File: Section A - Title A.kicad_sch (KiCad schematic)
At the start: 0 parts

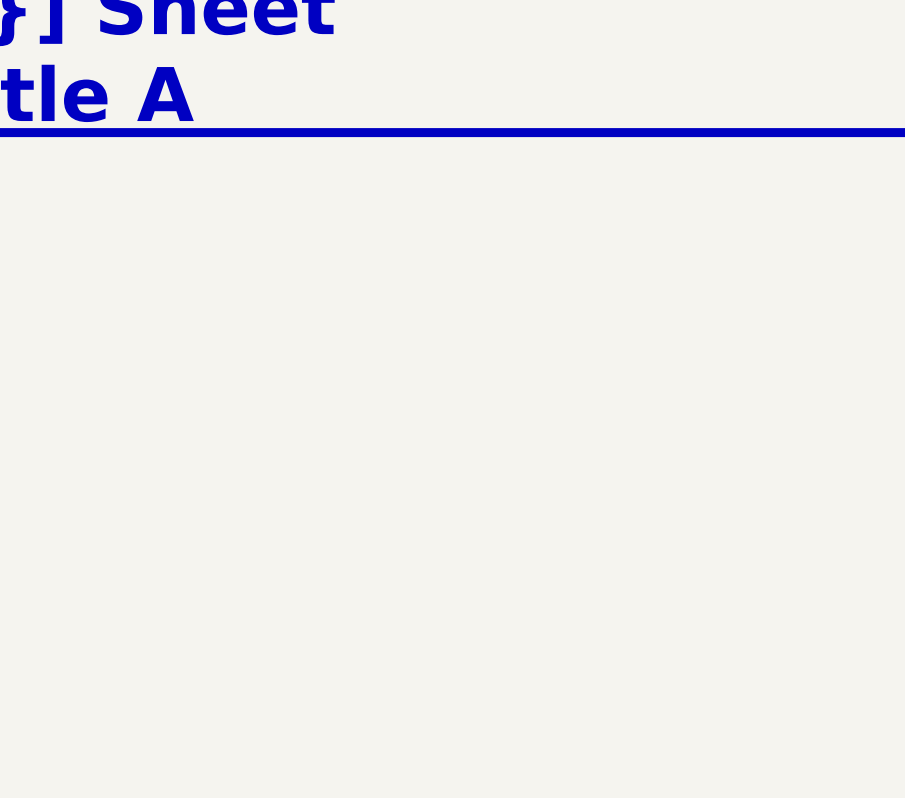
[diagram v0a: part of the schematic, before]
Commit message: Starter board, JLCPCB order files, PR checks, outputs branch, --init
- Starter board: 40x30 mm outline, H1-H4 mounting holes, TP1 on GND
  (ERC/DRC/parity clean), real dimensions, so every status works from the
  first run. KDT example dimensions for another board removed.
- Impedance tables from the JLCPCB calculator, stored in the stackup
  profiles and written by --stackup (JLC04161H-7628 / JLC06161H-3313).
- JLCPCB order files (KiBot JLCPCB template): Gerbers ZIP, BoM with LCSC
  part numbers, pick and place with rotation corrections. LCSC column in
  the regular BoMs.
- CI: pull request checks (pr_variant, ERC/DRC) with a summary comment,
  job summary on every run, outputs published to kibot-outputs/<branch>
  (ci_outputs: branch | commit | none) instead of growing the history.
- ./run_kibot.sh --init sets the metadata and renames the project files;
  GIT_URL: auto uses the git remote. DRAFT README generated after the text
  variables update.
- Generated outputs committed by the first CI runs removed from the template.

Co-Authored-By: Claude Opus 5.5 (1M context) <noreply@anthropic.com>
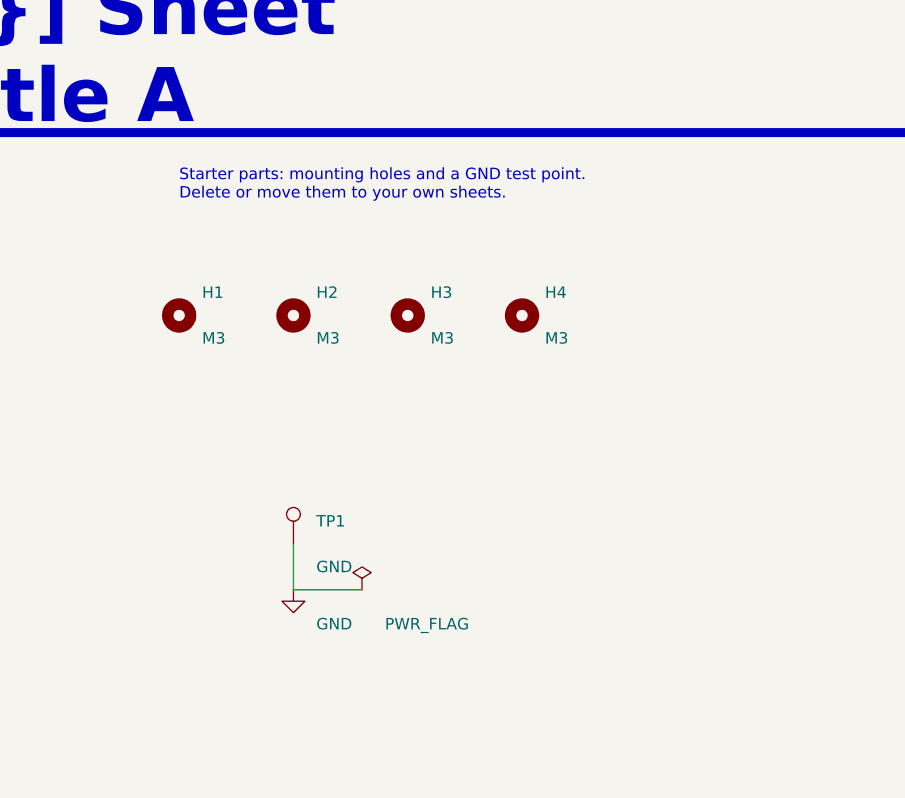
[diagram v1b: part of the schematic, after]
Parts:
- added H1, H2, H3, H4: M3, MountingHole:MountingHole_3.2mm_M3, symbol Mechanical:MountingHole
- added TP1: GND, TestPoint:TestPoint_THTPad_D1.5mm_Drill0.7mm, symbol Connector:TestPoint
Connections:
- new net GND: TP1.1
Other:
- note added: "Starter parts: mounting holes and a GND test point. Delete or move them to your own sheets."
